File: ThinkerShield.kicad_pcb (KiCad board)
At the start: 2 copper layers, 69 x 69 mm, 48 parts, among them SW1 SW_PUSHBUTTON, SW2 SW_PUSHBUTTON, U1 BUZZER

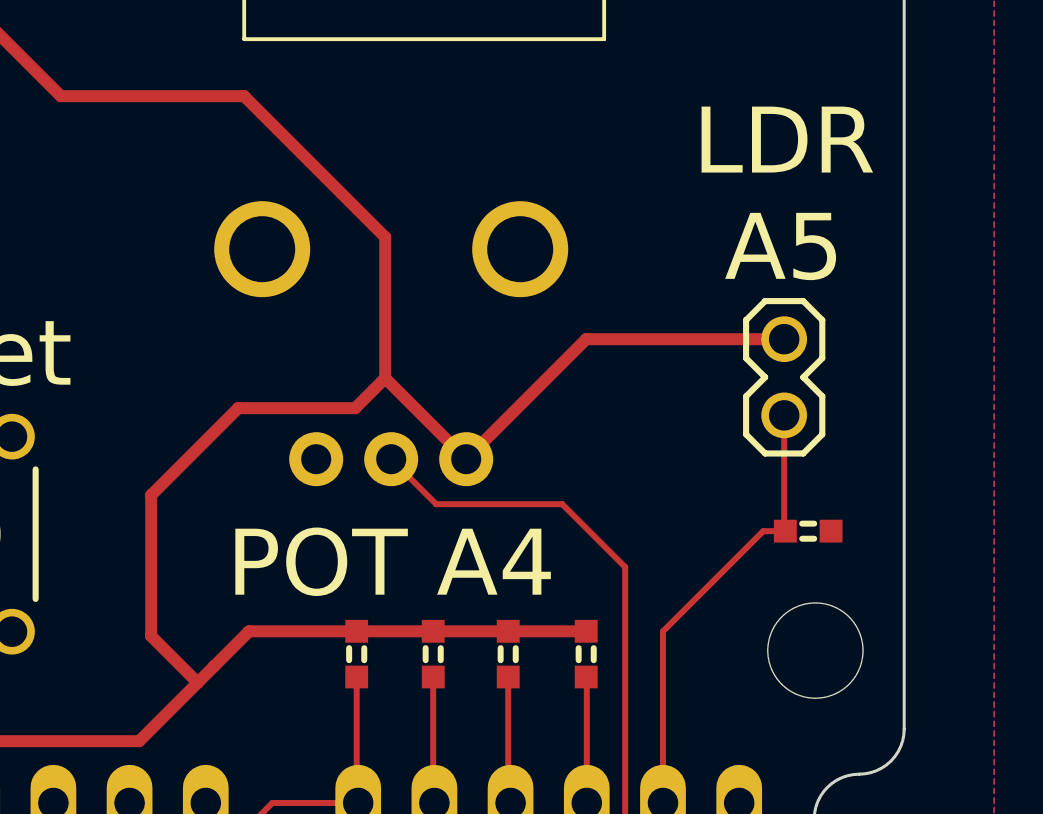
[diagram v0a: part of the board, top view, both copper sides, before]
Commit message: Update silkscreen A4/A5 swap to match electrical connections, bump version to 1.2
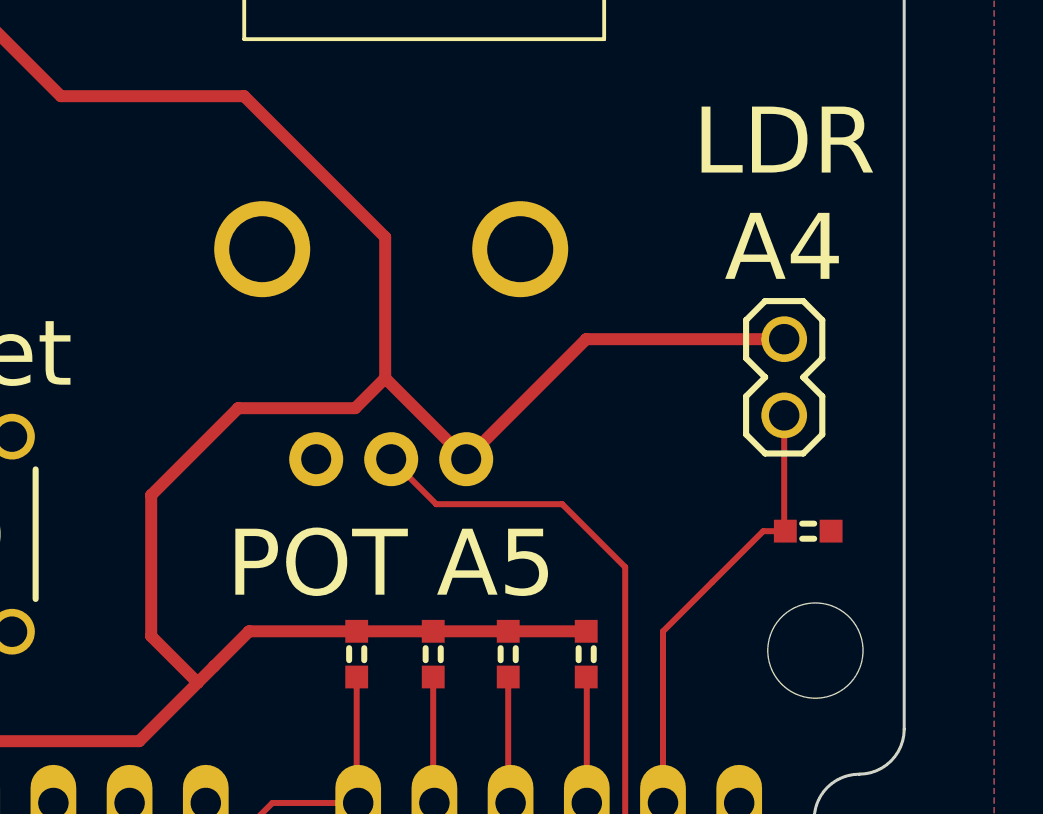
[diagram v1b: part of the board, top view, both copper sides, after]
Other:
- board text added: "LDR A4"
- board text added: "POT A5"
- board text added: "ThinkerShield V1.2"
- board text removed: "LDR A5"
- board text removed: "POT A4"
- board text removed: "ThinkerShield V1.1"
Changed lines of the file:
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@@
-(kicad_pcb (version 4) (host pcbnew 0.201508060901+6055~28~ubuntu15.04.1-product)
+(kicad_pcb (version 4) (host pcbnew 0.201509280902+6225~30~ubuntu15.10.1-product)
   (general
     (links 87)
@@
   (page A4)
   (layers
-    (0 F.Cu signal hide)
+    (0 F.Cu signal)
     (31 B.Cu signal hide)
     (32 B.Adhes user)
@@
     (34 B.Paste user)
     (35 F.Paste user hide)
-    (36 B.SilkS user hide)
+    (36 B.SilkS user)
     (37 F.SilkS user)
     (38 B.Mask user hide)
@@
   )
   (module FT:FIDUCIAL (layer F.Cu)
+    (at 205 93.5)
+    (descr "Quartz boitier HC-49 Vertical")
+    (tags "QUARTZ DEV")
+    (autoplace_cost180 10)
+    (fp_text reference FIDUCIAL (at 0.025 -0.3) (layer F.SilkS) hide
+      (effects (font (size 0.127 0.127) (thickness 0.03175)))
+    )
+    (fp_text value val** (at 0.025 0.3) (layer F.SilkS) hide
+      (effects (font (size 0.127 0.127) (thickness 0.03175)))
+    )
+    (pad FID smd circle (at 0 0) (size 1 1) (layers F.Cu F.Mask)
+      (solder_mask_margin 1) (clearance 1.00076))
+  )
+  (module FT:FIDUCIAL (layer F.Cu)
     (at 221 71)
     (descr "Quartz boitier HC-49 Vertical")
@@
       (effects (font (size 0.127 0.127) (thickness 0.03175)))
     )
-    (pad FID smd circle (at 0 0) (size 1 1) (layers F.Cu F.Paste F.Mask)
+    (pad FID smd circle (at 0 0) (size 1 1) (layers F.Cu F.Mask)
       (solder_mask_margin 1) (clearance 1.00076))
   )
@@
       (effects (font (size 0.127 0.127) (thickness 0.03175)))
     )
-    (pad FID smd circle (at 0 0) (size 1 1) (layers F.Cu F.Paste F.Mask)
-      (solder_mask_margin 1) (clearance 1.00076))
-  )
-  (module FT:FIDUCIAL (layer F.Cu)
-    (at 205 93.5)
-    (descr "Quartz boitier HC-49 Vertical")
-    (tags "QUARTZ DEV")
-    (autoplace_cost180 10)
-    (fp_text reference FIDUCIAL (at 0.025 -0.3) (layer F.SilkS) hide
-      (effects (font (size 0.127 0.127) (thickness 0.03175)))
-    )
-    (fp_text value val** (at 0.025 0.3) (layer F.SilkS) hide
-      (effects (font (size 0.127 0.127) (thickness 0.03175)))
-    )
-    (pad FID smd circle (at 0 0) (size 1 1) (layers F.Cu F.Paste F.Mask)
+    (pad FID smd circle (at 0 0) (size 1 1) (layers F.Cu F.Mask)
       (solder_mask_margin 1) (clearance 1.00076))
   )
@@
     (effects (font (size 1.2 1.2) (thickness 0.3)) (justify left mirror))
   )
-  (gr_text "LDR\nA5" (at 233 82.2) (layer F.SilkS)
+  (gr_text "LDR\nA4" (at 233 82.2) (layer F.SilkS)
     (effects (font (size 2.2 2.2) (thickness 0.45)))
   )
-  (gr_text "ThinkerShield V1.1" (at 229 70) (layer B.SilkS)
+  (gr_text "ThinkerShield V1.2" (at 229 70) (layer B.SilkS)
     (effects (font (size 2 2) (thickness 0.5)) (justify left mirror))
   )
@@
     (effects (font (size 1.2 1.2) (thickness 0.3)) (justify left mirror))
   )
-  (gr_text "POT A4" (at 219.9 94.5) (layer F.SilkS)
+  (gr_text "POT A5\n" (at 219.9 94.5) (layer F.SilkS)
     (effects (font (size 2.2 2.2) (thickness 0.45)))
   )
